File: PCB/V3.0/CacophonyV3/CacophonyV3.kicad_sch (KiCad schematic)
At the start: 25 parts, among them J1 Conn_01x04, J2 Conn_01x05, J3 Conn_01x03, J4 Conn_01x03, J5 Conn_01x03, J6 Conn_01x02

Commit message: Added PCBv3
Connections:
- net +3.3V: now also IC1.2 (+5)
- net +5V: no longer IC1.2 (+5)
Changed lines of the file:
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@@
 			)
 		)
-		(property "Value" "+5V"
+		(property "Value" "+3.3V"
 			(at 49.53 85.0899 90)
 			(effects

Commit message: New PCB
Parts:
- added R101: 200k, Resistor_SMD:R_0402_1005Metric, symbol Device:R
- added R102: 100k, Resistor_SMD:R_0402_1005Metric, symbol Device:R
- C1, C2, C3, C4: footprint Capacitor_SMD:C_1206_3216Metric -> Resistor_SMD:R_0402_1005Metric
- D4, D5: footprint LED_SMD:LED_0603_1608Metric -> LED_SMD:LED_0402_1005Metric
- R10, R11, R12, R6, R8, R9: footprint Resistor_SMD:R_2512_6332Metric -> Resistor_SMD:R_0402_1005Metric
- R7: footprint Resistor_SMD:R_2512_6332Metric -> Capacitor_SMD:C_0402_1005Metric
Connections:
- net +3.3V: no longer IC1.2 (+5)
- net +5V: now also IC1.2 (+5)
- net +9V: now also R101.1
- net GND: now also R102.2
- net PWM_L: now also U1.13 (IO12); no longer U1.14 (IO11)
- net PWM_R: now also U1.14 (IO11); no longer U1.13 (IO12)
- net VOut: now reaches U1.5 (IO2)
- net VOut: now also R101.2, R102.1
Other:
- note added: "ESP"
- note added: "Power"
- note added: "Pullups"
- note added: "Servo"
- moved on the sheet: B1, B2, C1, C2, C3, C4, D2, D3, D4, D5, IC1, J1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

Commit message: PCBv3 Fabrication
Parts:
- R11, R12: value 10k -> 1k
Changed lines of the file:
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@@
 			)
 		)
-		(property "Value" "10k"
+		(property "Value" "1k"
 			(at 222.25 83.82 90)
 			(effects
@@
 			)
 		)
-		(property "Value" "10k"
+		(property "Value" "1k"
 			(at 220.98 73.66 90)
 			(effects

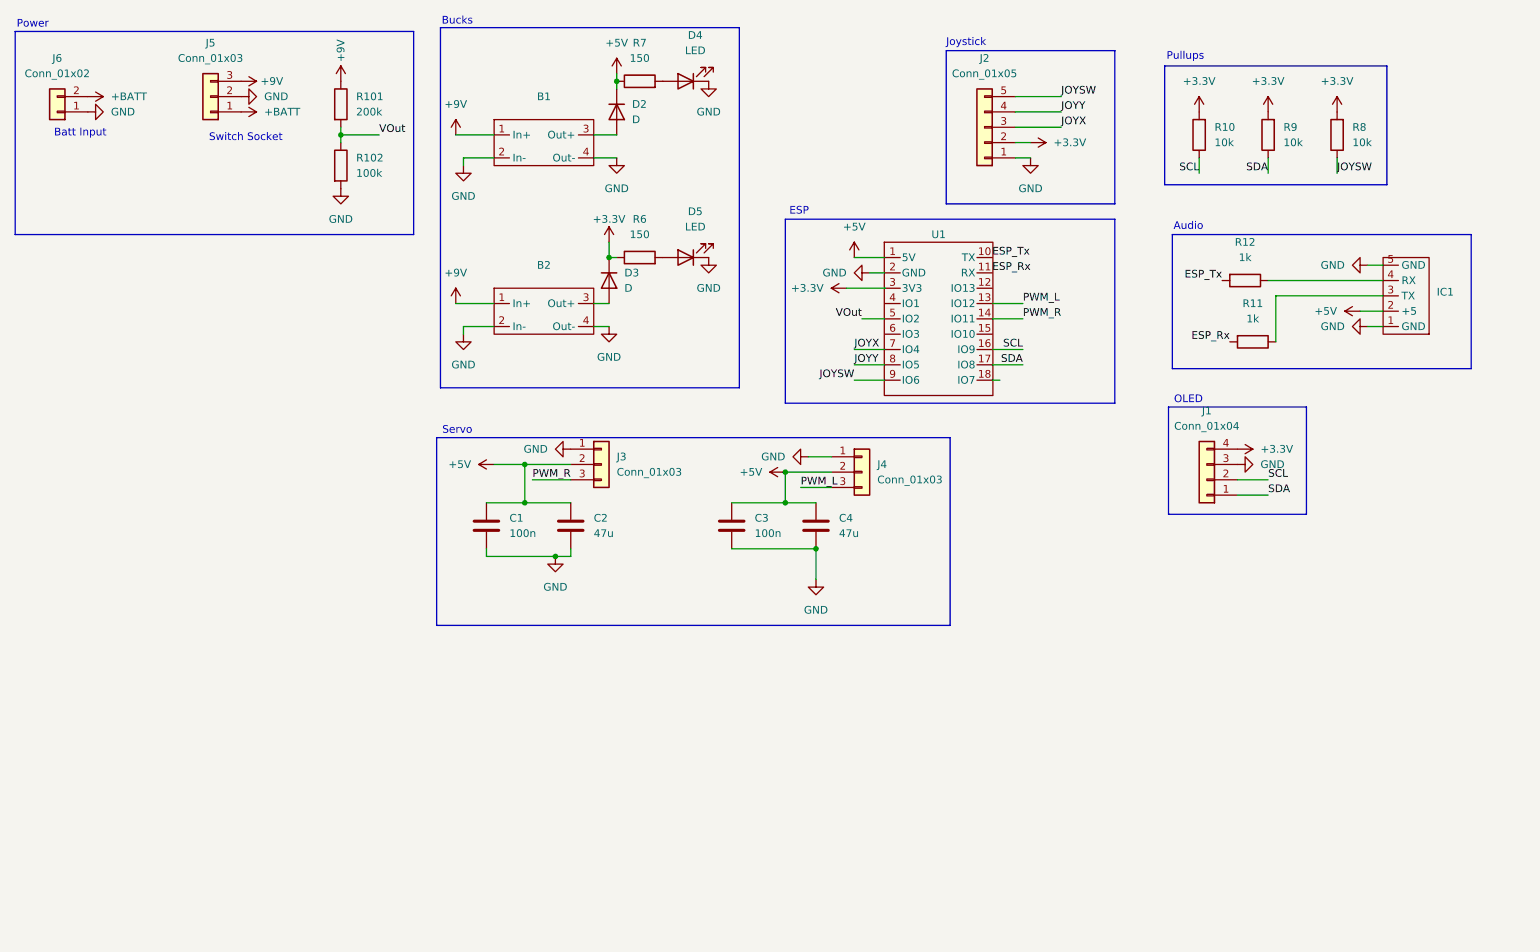
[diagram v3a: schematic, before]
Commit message: SImplified UI, fixed JS
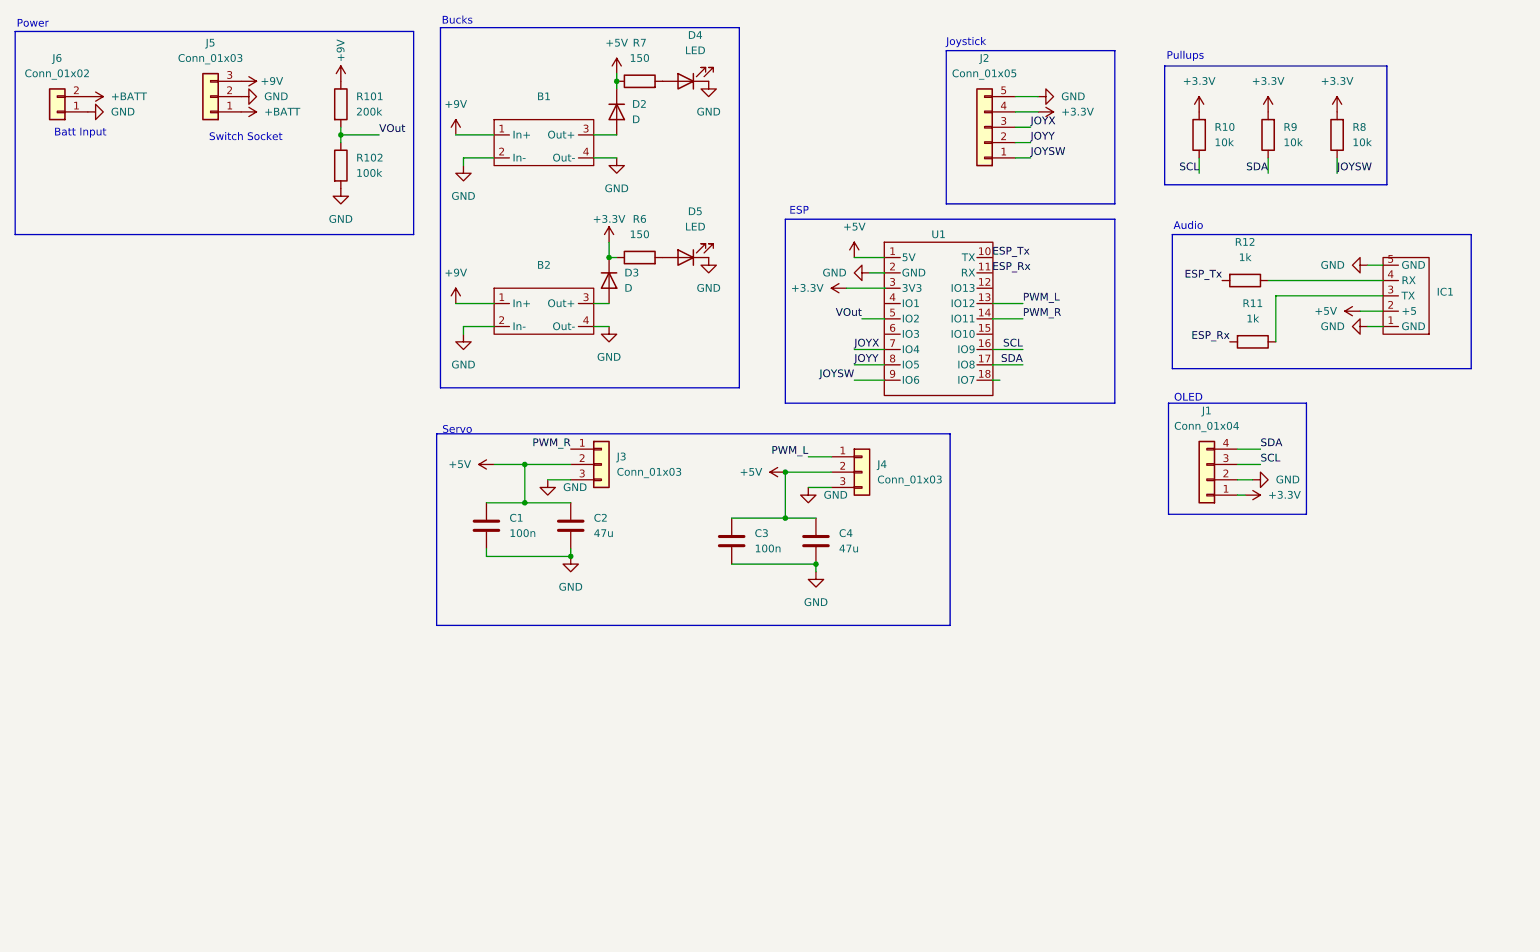
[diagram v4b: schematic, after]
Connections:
- net +3.3V: now also J1.1 (Pin_1), J2.4 (Pin_4); no longer J1.4 (Pin_4), J2.2 (Pin_2)
- net GND: now also J1.2 (Pin_2), J2.5 (Pin_5), J3.3 (Pin_3), J4.3 (Pin_3); no longer J1.3 (Pin_3), J2.1 (Pin_1), J3.1 (Pin_1), J4.1 (Pin_1)
- net JOYSW: now also J2.1 (Pin_1); no longer J2.5 (Pin_5)
- net JOYY: now also J2.2 (Pin_2); no longer J2.4 (Pin_4)
- net PWM_L: now also J4.1 (Pin_1); no longer J4.3 (Pin_3)
- net PWM_R: now also J3.1 (Pin_1); no longer J3.3 (Pin_3)
- net SCL: now also J1.3 (Pin_3); no longer J1.2 (Pin_2)
- net SDA: now also J1.4 (Pin_4); no longer J1.1 (Pin_1)
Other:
- moved on the sheet: C3, C4
